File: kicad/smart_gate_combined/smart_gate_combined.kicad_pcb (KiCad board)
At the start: 2 copper layers, 201.7 x 119.6 mm, 31 parts

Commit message: fix(kicad): remove pcbnew.ImportSpecctraSES — shifted everything via aux origin
KiCad 6's ImportSpecctraSES applies an internal aux-origin offset when
re-importing the SES that ExportSpecctraDSN added during export. Effect:
footprints + edge cuts ended up shifted ~28-83 mm in X/Y after a roundtrip,
making the GND pour (placed at script coordinates) appear misaligned vs
the board outline (which had drifted).

Fix: autoroute.py no longer calls ImportSpecctraSES. Custom import_ses.py
parses the SES coordinates directly and adds tracks without touching
footprint positions.

After full pipeline re-run:
  Edge.Cuts: X [100, 350], Y [100, 250]  (correct, 250x150mm)
  H1: (105, 105)                          (correct)
  GND zone: (100.5, 100.5) -> (349.5, 249.5)  (aligned)
  355 tracks + 10 vias

Co-Authored-By: Claude Opus 4.7 <noreply@anthropic.com>
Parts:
- removed FB_PI: FB_600R_3A, L_Axial_L11.0mm_D4.5mm_P15.24mm_Horizontal_Fastron_MECC
- moved J_EXP 234.7 mm to (120.0, 230.0), turned to 0 degrees
- moved J_ESP 156.5 mm to (192.0, 200.0), turned to 90 degrees
- moved H4 136.0 mm to (345.0, 245.0)
- moved R_SDA 120.9 mm to (278.0, 165.0), turned to 0 degrees
- moved H3 116.3 mm to (105.0, 245.0)
- moved H2 112.2 mm to (345.0, 105.0)
- moved C_BULK 108.8 mm to (115.0, 155.0)
- moved J_PWR 107.2 mm to (115.0, 140.0)
- moved J_RFID 103.4 mm to (250.0, 150.0)
- moved J_BUCK 99.3 mm to (150.0, 160.0), turned to 0 degrees
- moved R_USR2 99.2 mm to (310.0, 165.0), turned to 0 degrees
- moved Q_BUZ 98.8 mm to (260.0, 200.0), turned to 0 degrees
- moved R_SCL 98.4 mm to (283.0, 165.0), turned to 0 degrees
- moved D_REV 93.8 mm to (130.0, 140.0), turned to 0 degrees
- moved J_BUZ 91.7 mm to (280.0, 200.0), turned to 0 degrees
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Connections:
- C_PI_BULK pad 1: PI_5V_FILTERED -> +5V
- C_PI_BYP pad 1: PI_5V_FILTERED -> +5V
- D_TVS pad 2: PI_5V_FILTERED -> +5V
- J_PI pad 2: PI_5V_FILTERED -> +5V
- J_PI pad 4: PI_5V_FILTERED -> +5V
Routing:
- net +5V: track 252.2 -> 379.7 mm, vias 0 -> 3
- net GND: track 587.0 -> 703.4 mm, vias 3 -> 0
- net RC522_MOSI: track 28.5 -> 124.7 mm, vias 0 -> 1
- net SERVO_PWM: track 71.5 -> 139.0 mm
- net +3V3: track 228.3 -> 293.5 mm, vias 1 -> 3
- net HCSR_ECHO_3V3: track 67.2 -> 5.16 mm
- net PI_5V_FILTERED: track 55.1 -> 0.00 mm
- net HCSR_TRIG: track 64.4 -> 117.9 mm
- net I2C_SDA: track 68.7 -> 101.7 mm
- net I2C_SCL: track 87.5 -> 116.0 mm
- net RC522_MISO: track 54.9 -> 82.3 mm, vias 0 -> 1
- net RC522_SCK: track 81.1 -> 106.8 mm
- net IO36: track 64.0 -> 86.6 mm
- net N$1: track 9.64 -> 31.8 mm
- net IO39: track 70.2 -> 90.2 mm
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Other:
- board size 201.7 x 119.6 mm -> 250 x 150 mm

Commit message: pivot(kicad): align pin map with firmware decision #26 + restore manual placement
Decision #26 (from smart_gate_uart_decision.md): Pi <-> ESP32 link is now
a 3-wire UART on PCB traces (not USB-C cable):
  - Pi pin 8  (BCM14, UART0 TX) -> ESP32 GPIO 32 (UART1 RX)
  - Pi pin 10 (BCM15, UART0 RX) <- ESP32 GPIO 25 (UART1 TX)
  - Pi pin 6 GND <-> ESP32 GND

Pin map remapping to free 32/25:
  - I2C SDA:    GPIO 32 -> GPIO 15 (strap HIGH, idle HIGH OK with pull-up)
  - HC-SR04 TRIG: GPIO 25 -> GPIO 4 (was RC522 RST, no strap concern)
  - RC522 CS:   GPIO 15 -> GPIO 5  (firmware-aligned)
  - RC522 RST:  GPIO 4  -> GPIO 17 (firmware-aligned)

Process:
1. Restored PCB from ~/Downloads/smart_gate_combined.kicad_pcb (user's manual placement)
2. Updated SKiDL pin assignments in build_combined.py
3. Regenerated netlist (FB_PI already removed)
4. Imported netlist into existing PCB — preserved 31 footprint positions
5. Re-routed (324 tracks, 91% B.Cu, 4 vias) + GND pour on F.Cu

Result: manual placement preserved; UART traces added per #26; all positions
exactly match the user's pre-rebuild arrangement.

Co-Authored-By: Claude Opus 4.7 <noreply@anthropic.com>
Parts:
- added FB_PI: FB_600R_3A, L_Axial_L11.0mm_D4.5mm_P15.24mm_Horizontal_Fastron_MECC, F.Cu at (195.6, 127.0)
- moved J_EXP 234.7 mm to (251.5, 35.6), turned to 90 degrees
- moved J_ESP 156.5 mm to (218.4, 45.7), turned to 0 degrees
- moved H4 136.0 mm to (269.2, 132.1)
- moved R_SDA 120.9 mm to (246.4, 48.3), turned to -90 degrees
- moved H3 116.3 mm to (77.3, 132.1)
- moved H2 112.2 mm to (269.0, 22.5)
- moved C_BULK 108.8 mm to (76.2, 53.3)
- moved J_PWR 107.2 mm to (84.7, 37.1)
- moved J_RFID 103.4 mm to (259.1, 47.0)
- moved J_BUCK 99.3 mm to (86.4, 83.8), turned to -90 degrees
- moved R_USR2 99.2 mm to (246.4, 88.9), turned to 90 degrees
- moved Q_BUZ 98.8 mm to (236.2, 104.1), turned to 180 degrees
- moved R_SCL 98.4 mm to (246.4, 73.7), turned to 90 degrees
- moved D_REV 93.8 mm to (94.0, 53.3), turned to 90 degrees
- moved J_BUZ 91.7 mm to (236.2, 119.4), turned to -90 degrees
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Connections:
- J_ESP pad 13: I2C_SDA -> PI_TX_ESP_RX
- J_ESP pad 17: HCSR_TRIG -> ESP_TX_PI_RX
- J_ESP pad 20: RC522_CS -> I2C_SDA
- J_ESP pad 24: RC522_RST -> HCSR_TRIG
- J_ESP pad 28: ESP_TX_PI_RX -> RC522_RST
- J_ESP pad 30: PI_TX_ESP_RX -> RC522_CS
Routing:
- net GND: track 703.4 -> 566.1 mm
- net RC522_SCK: track 106.8 -> 0.00 mm
- net HCSR_TRIG: track 117.9 -> 42.6 mm
- net I2C_SCL: track 116.0 -> 42.7 mm
- net I2C_SDA: track 101.7 -> 32.2 mm, vias 0 -> 1
- net PI_TX_ESP_RX: track 65.3 -> 0.00 mm, vias 1 -> 0
- net HCSR_ECHO_3V3: track 5.16 -> 68.8 mm
- net SERVO_PWM: track 139.0 -> 76.5 mm
- net +3V3: track 293.5 -> 236.9 mm, vias 3 -> 1
- net RC522_MOSI: track 124.7 -> 84.3 mm, vias 1 -> 0
- net RC522_MISO: track 82.3 -> 54.9 mm, vias 1 -> 0
- net +5V: track 379.7 -> 406.4 mm, vias 3 -> 1
- net N$1: track 31.8 -> 9.64 mm
- net IO36: track 86.6 -> 65.3 mm
- net IO39: track 90.2 -> 71.1 mm
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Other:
- board size 250 x 150 mm -> 201.7 x 119.6 mm

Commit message: fix(kicad): auto-fit GND pour to actual Edge.Cuts + 0.7mm track width
User reported pour misaligned after restoring backup PCB whose outline
sits at (72.3,17.5)->(274.0,137.1) due to the earlier ImportSpecctraSES
roundtrip-shift. The pour was hardcoded to pcb_common.BOARD_ORIGIN_X/Y
constants (100/100) which no longer match the board.

Fixes:
- add_gnd_pour.py reads Edge.Cuts geometry from the loaded board to
  derive the zone outline at runtime — always fits whatever rectangle
  KiCad has on Edge.Cuts.
- import_ses.py overrides SES-encoded 0.25mm track width to 0.7mm
  uniformly via FORCE_TRACK_WIDTH_NM constant.

After re-route:
  Board outline: (72.3,17.5)->(274.0,137.1)
  Zone outline:  (72.8,18.0)->(273.5,136.6)  (0.5mm margin)
  386 tracks @ 0.7mm + 13 vias

Co-Authored-By: Claude Opus 4.7 <noreply@anthropic.com>
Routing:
- net RC522_SCK: track 0.00 -> 112.2 mm
- net I2C_SCL: track 42.7 -> 152.4 mm
- net HCSR_ECHO_3V3: track 68.8 -> 140.5 mm
- net I2C_SDA: track 32.2 -> 62.4 mm, vias 1 -> 4
- net +3V3: track 236.9 -> 221.6 mm, vias 1 -> 3
- net RC522_MOSI: track 84.3 -> 72.0 mm, vias 0 -> 1
- net IO39: track 71.1 -> 60.9 mm
- net +5V: track 406.4 -> 397.8 mm, vias 1 -> 3
- net ESP_TX_PI_RX: track 50.6 -> 42.7 mm
- net RC522_CS: track 55.3 -> 61.8 mm
- net N$2: track 24.5 -> 30.9 mm, vias 0 -> 1
- net BUZ_DRIVE: track 60.7 -> 64.7 mm, vias 1 -> 2
- net IO36: track 65.3 -> 62.5 mm
- net RC522_RST: track 36.0 -> 38.5 mm
- net GND: track 566.1 -> 564.2 mm, vias 0 -> 2
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
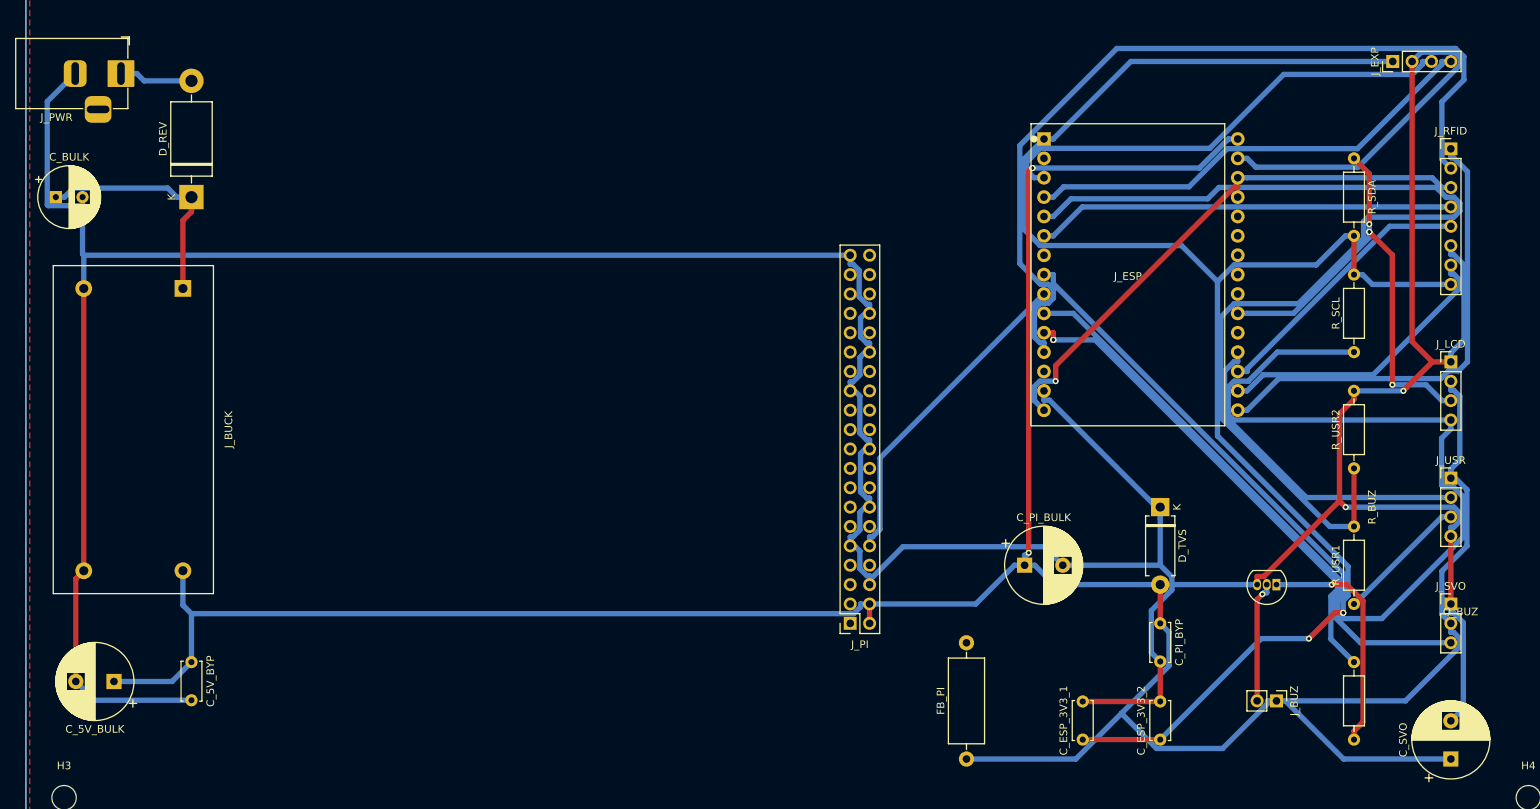
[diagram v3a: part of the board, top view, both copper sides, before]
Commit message: tune(kicad): track width 1.0mm — prevents routing between component pins
User asked to enlarge tracks to 1mm AND ensure tracks do not weave
between adjacent component pins (e.g., between pin 5 and 6 of a 1x15
header at 2.54mm pitch).

At 2.54mm pitch with 1.8mm pads, the gap between adjacent pad edges is
~0.74mm — a 1.0mm track + 0.2mm clearance needs 1.4mm minimum width to
fit. Physically impossible, so FreeRouting now routes AROUND component
pin clusters.

Changes:
- import_ses.py: FORCE_TRACK_WIDTH_NM = 1_000_000 (was 700_000)
- autoroute.py: DSN width override 250um -> 1000um before FreeRouting runs
  (so FreeRouting plans routes that actually fit at the new width)

Result: 286 tracks @ 1.0mm + 26 vias.
B.Cu still primary (79%); F.Cu rose to 21% because thicker tracks need
more cross-layer escapes — acceptable for THT prototype.

Co-Authored-By: Claude Opus 4.7 <noreply@anthropic.com>
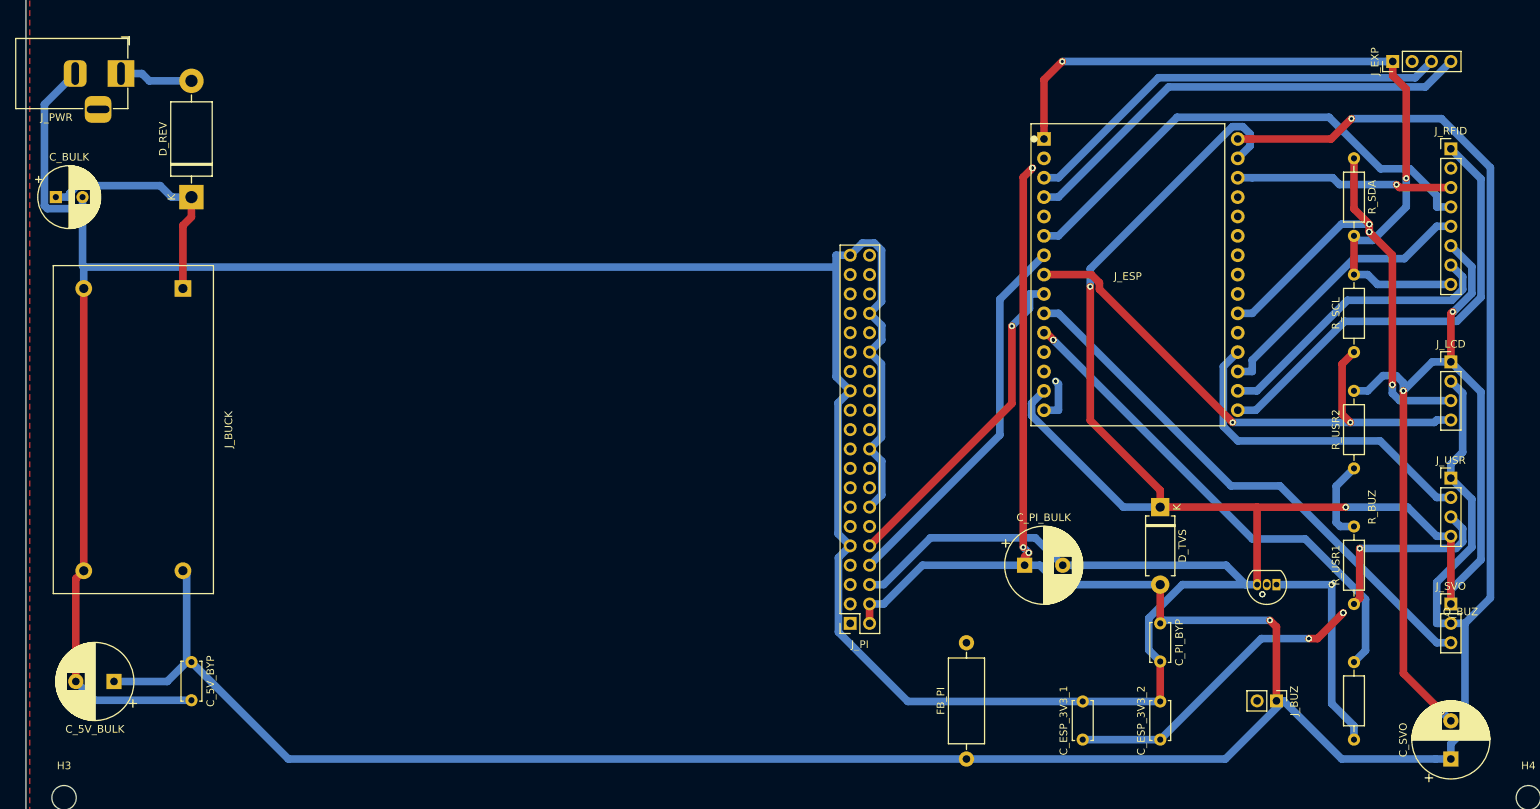
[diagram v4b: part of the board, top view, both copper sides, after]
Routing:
- net GND: track 564.2 -> 695.6 mm, vias 2 -> 7
- net HCSR_ECHO_3V3: track 140.5 -> 10.6 mm
- net RC522_SCK: track 112.2 -> 0.00 mm
- net +5V: track 397.8 -> 484.8 mm, vias 3 -> 8
- net I2C_SCL: track 152.4 -> 72.3 mm, vias 0 -> 2
- net +3V3: track 221.6 -> 142.5 mm, vias 3 -> 7
- net PI_TX_ESP_RX: track 0.00 -> 50.1 mm
- net RC522_MOSI: track 72.0 -> 34.3 mm, vias 1 -> 3
- net BUZ_COLLECTOR: track 16.0 -> 0.00 mm, vias 1 -> 2
- net RC522_MISO: track 54.9 -> 65.5 mm
- net HCSR_ECHO_5V: track 17.4 -> 25.4 mm, vias 0 -> 1
- net IO36: track 62.5 -> 57.1 mm
- net SERVO_PWM: track 75.2 -> 71.2 mm
- net RC522_CS: track 61.8 -> 59.1 mm
- net N$2: track 30.9 -> 28.8 mm, vias 1 -> 2
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
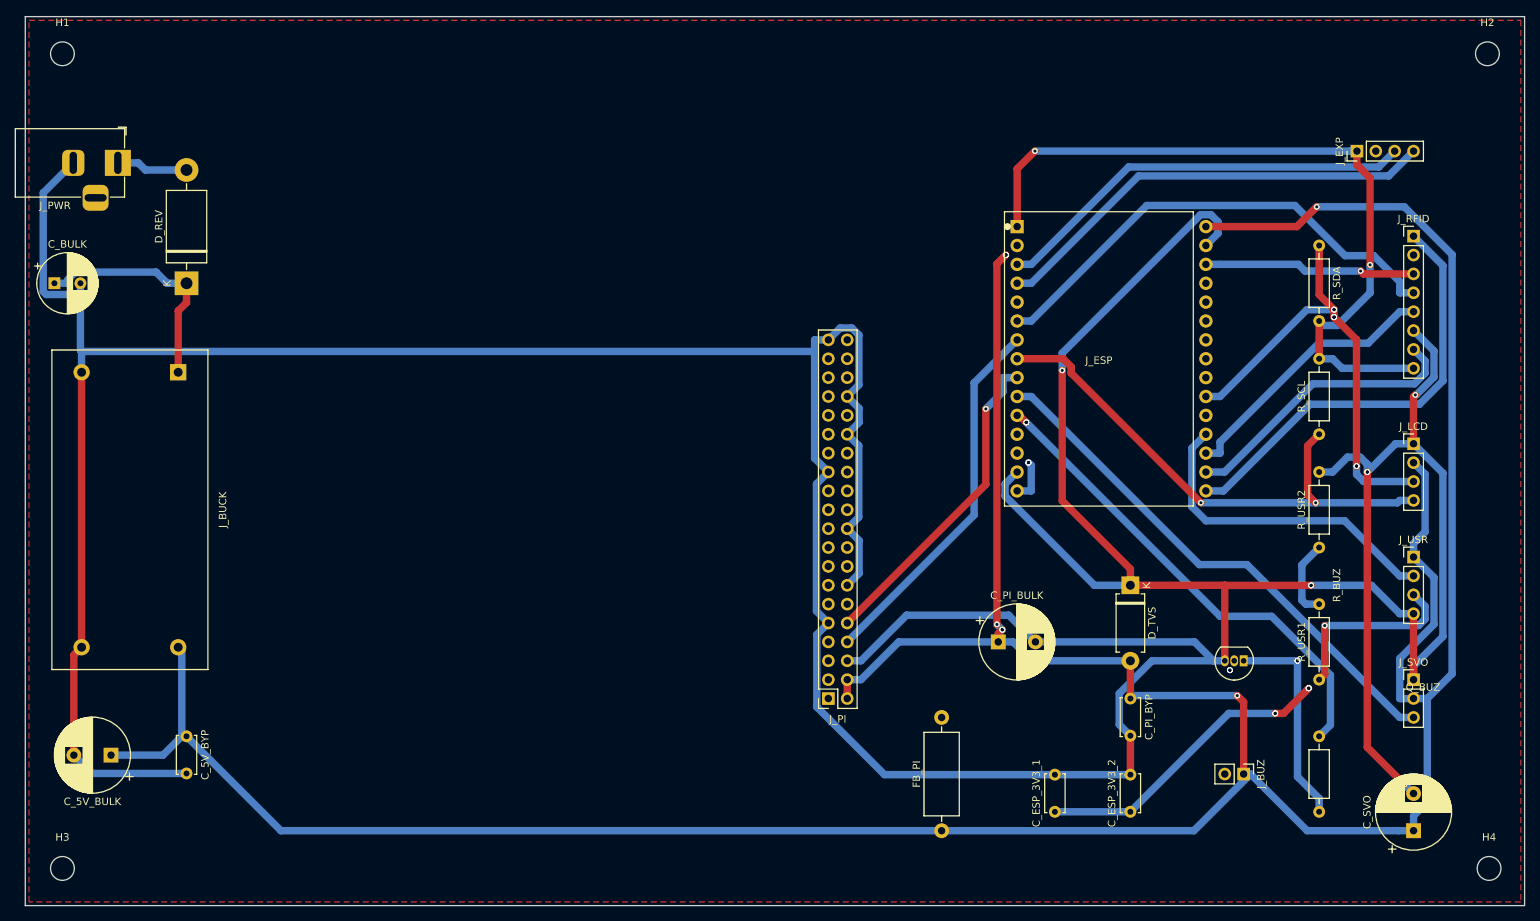
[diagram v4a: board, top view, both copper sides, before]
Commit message: route(kicad): full re-route with both layers, 50 passes, clearance 0.2mm
Best result after multiple iterations:
- Both F.Cu + B.Cu signal routing (was B.Cu-only — too tight at 1mm width)
- 50 max passes (was 20)
- Clearance 0.2mm in Default net class (was 0.4mm — overly strict)
- Dedupe duplicate same-net vias post-import

Result:
- 546 tracks (F.Cu 26%, B.Cu 74%) + 66 vias
- 44 DRC violations: 2 errors (unconnected BUZ_COLLECTOR), 42 warnings
- 38 via_dangling warnings (Local override severity)
- 2 unconnected_items in buzzer area — user to route manually

Removed:
- 4 PCB_DIM_ALIGNED dimension annotations (caused edge_clearance error)
- 58 duplicate vias

Co-Authored-By: Claude Opus 4.7 <noreply@anthropic.com>
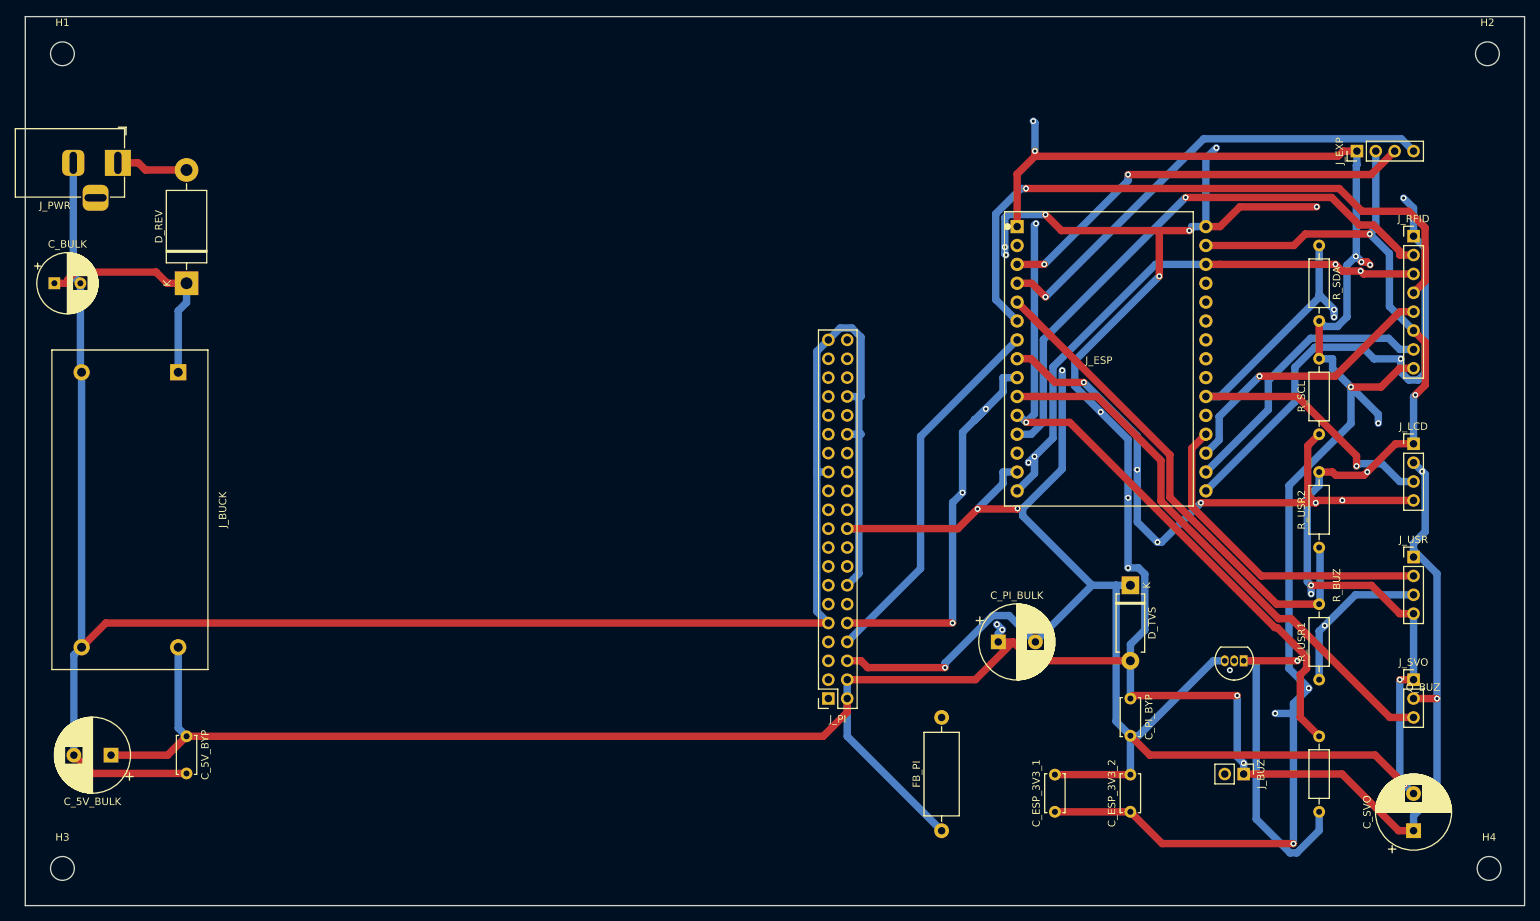
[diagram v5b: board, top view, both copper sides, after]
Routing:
- net +3V3: track 142.5 -> 219.5 mm, vias 7 -> 10
- net RC522_SCK: track 0.00 -> 76.5 mm, vias 0 -> 1
- net GND: track 695.6 -> 632.5 mm, vias 7 -> 11
- net HCSR_ECHO_3V3: track 10.6 -> 68.5 mm
- net +5V: track 484.8 -> 430.4 mm, vias 8 -> 16
- net RC522_MOSI: track 34.3 -> 74.6 mm, vias 3 -> 4
- net BUZ_DRIVE: track 65.5 -> 91.8 mm, vias 3 -> 2
- net RC522_MISO: track 65.5 -> 86.4 mm, vias 0 -> 1
- net N$2: track 28.8 -> 44.2 mm, vias 2 -> 1
- net I2C_SCL: track 72.3 -> 83.0 mm, vias 2 -> 6
- net ESP_TX_PI_RX: track 43.6 -> 54.0 mm, vias 1 -> 3
- net RC522_CS: track 59.1 -> 68.2 mm, vias 0 -> 2
- net HCSR_ECHO_5V: track 25.4 -> 21.3 mm
- net SERVO_PWM: track 71.2 -> 74.4 mm
- net IO39: track 60.7 -> 63.6 mm, vias 0 -> 1
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- removed copper zone on F.Cu, net GND
